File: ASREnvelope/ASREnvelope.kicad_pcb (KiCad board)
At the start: 2 copper layers, 40 parts, among them J1 GATE, J2 Power, J3 OUT, J4 INV OUT, U1 TL074, U2 TL072

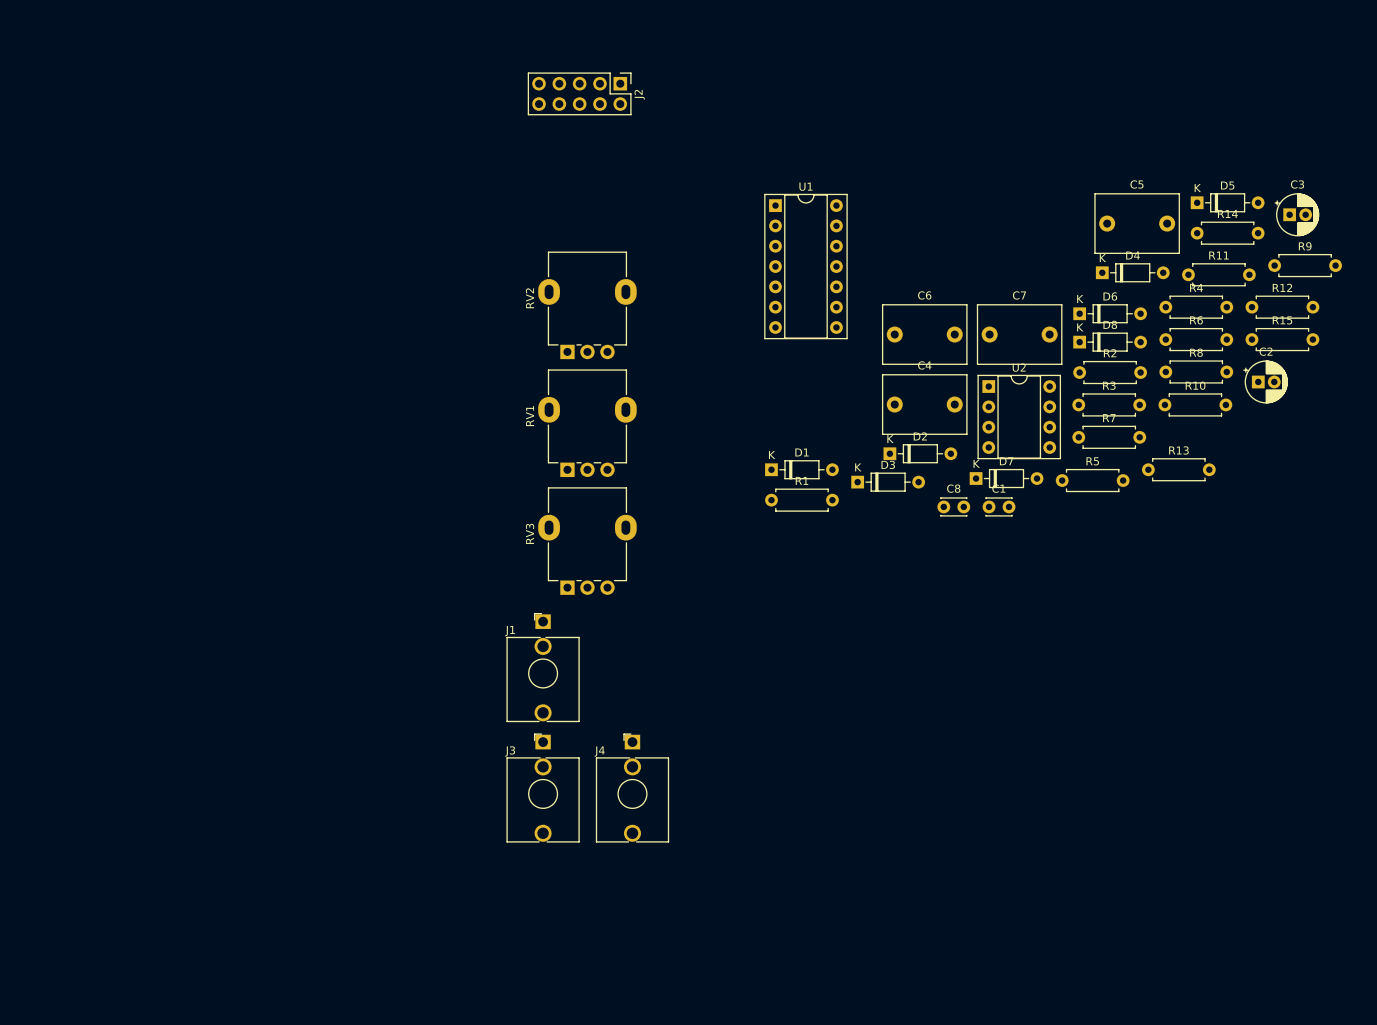
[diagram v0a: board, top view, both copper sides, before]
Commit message: move circuit to two boards
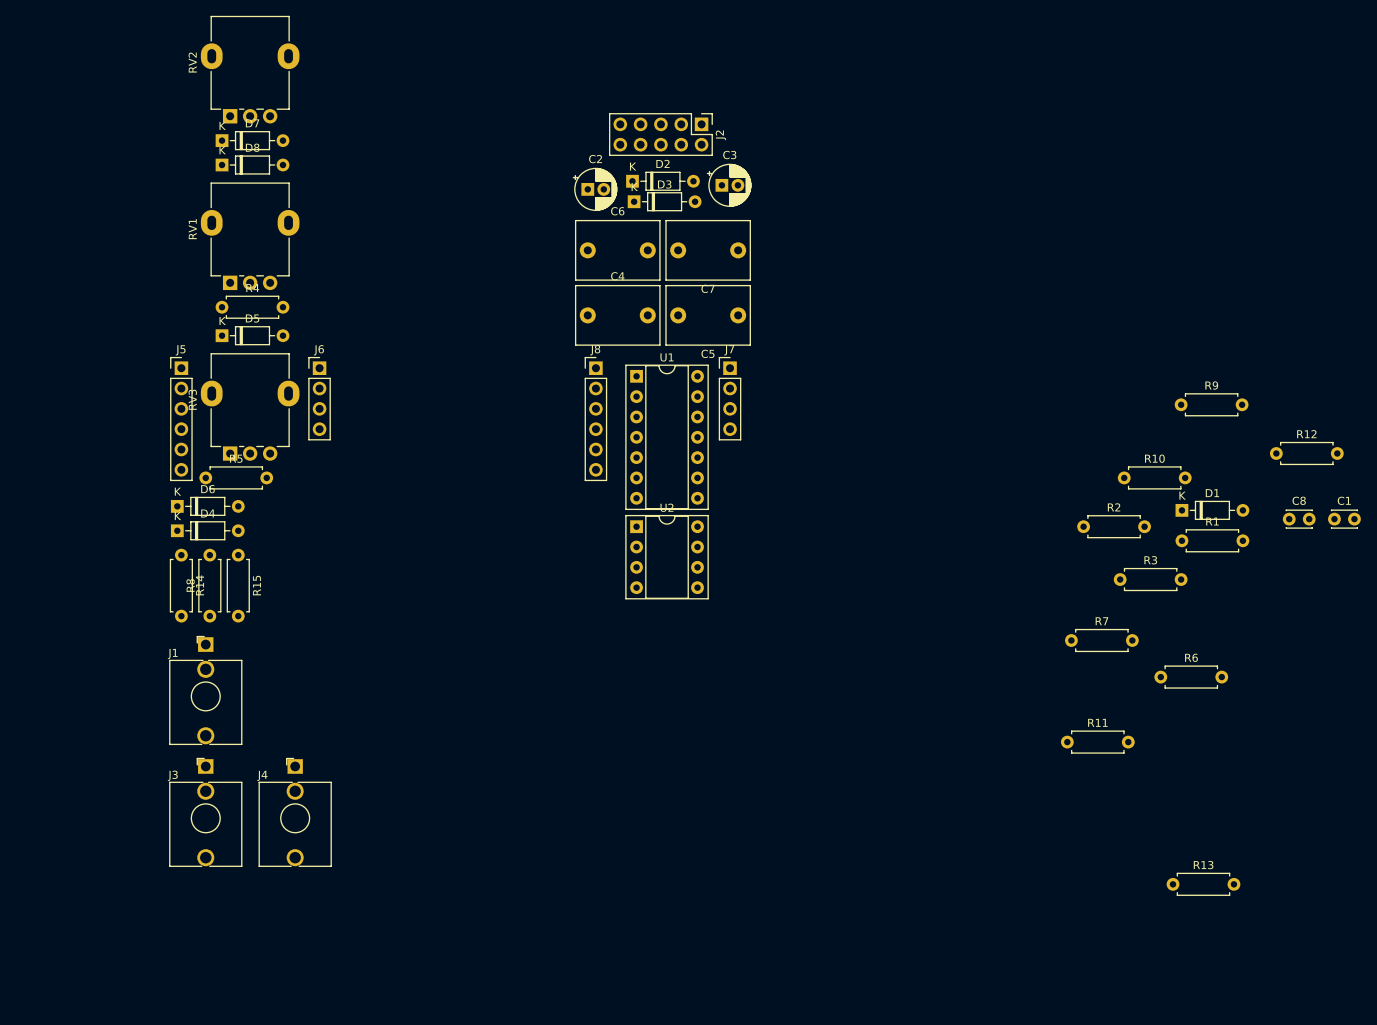
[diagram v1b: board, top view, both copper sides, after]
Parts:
- added J5: Conn_01x06_Male, Connector_PinHeader_2.54mm:PinHeader_1x06_P2.54mm_Vertical, F.Cu at (108.2, 79.2)
- added J6: Conn_01x04_Male, Connector_PinHeader_2.54mm:PinHeader_1x04_P2.54mm_Vertical, F.Cu at (125.5, 79.2)
- added J7: Conn_01x04_Female, Connector_PinHeader_2.54mm:PinHeader_1x04_P2.54mm_Vertical, F.Cu at (176.8, 79.2)
- added J8: Conn_01x06_Female, Connector_PinHeader_2.54mm:PinHeader_1x06_P2.54mm_Vertical, F.Cu at (160.0, 79.2)
- moved R14 133.2 mm to (108.2, 102.6), turned to 270 degrees
- moved R15 129.5 mm to (115.3, 102.6), turned to 270 degrees
- moved R8 123.3 mm to (111.8, 110.2), turned to 90 degrees
- moved D5 123.0 mm to (113.3, 75.2)
- moved D4 120.0 mm to (107.7, 99.6)
- moved R4 118.0 mm to (113.3, 71.6)
- moved D6 115.3 mm to (107.7, 96.5)
- moved D8 109.5 mm to (113.3, 53.8)
- moved R5 107.1 mm to (111.3, 93.0)
- moved D7 103.3 mm to (113.3, 50.8)
- moved C2 87.2 mm to (159.0, 56.9)
- moved C3 71.1 mm to (175.8, 56.4)
- moved R11 60.3 mm to (218.9, 126.0)
- moved R13 51.9 mm to (232.2, 143.8)
- moved D1 51.6 mm to (233.3, 97.0)
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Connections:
- net Earth renamed GroundA
- C1 pad 2: Net-(C1-Pad2) -> GateJackB
- C8 pad 1: Net-(C8-Pad1) -> Conn4B
- D4 pad 2: Net-(D4-Pad2) -> Switch3A
- D5 pad 2: Net-(D5-Pad2) -> Conn1A
- D6 pad 2: Net-(D6-Pad2) -> Switch1A
- J1 pad T: Net-(C1-Pad2) -> GateJackA
- R11 pad 1: Net-(R11-Pad1) -> OutJackB
- R13 pad 2: Net-(R13-Pad2) -> InvOutJackB'
- R14 pad 1: Net-(R11-Pad1) -> OutJackA
- R15 pad 1: Net-(R13-Pad2) -> InvOutJackA
- R4 pad 1: Net-(D4-Pad1) -> Switch3A
- R6 pad 2: Net-(D6-Pad2) -> Switch1B
- R8 pad 2: Net-(R8-Pad2) -> Conn3A
- RV2 pad 1: Net-(C8-Pad1) -> Conn4A
- RV2 pad 2: Net-(C8-Pad1) -> Conn4A
- RV3 pad 1: Net-(C8-Pad1) -> Conn4A
- RV3 pad 2: Net-(C8-Pad1) -> Conn4A
- U1 pad 1: Net-(D4-Pad2) -> Switch3B
- U1 pad 10: Net-(SW1-Pad2) -> Switch2B
- U1 pad 13: Net-(R11-Pad1) -> OutJackB
- U1 pad 14: Net-(D6-Pad2) -> Switch1B
- U1 pad 5: Net-(C1-Pad2) -> GateJackB
- U1 pad 7: Net-(D5-Pad2) -> Conn1B
- U1 pad 8: Net-(R8-Pad2) -> Conn3B
- U1 pad 9: Net-(R8-Pad2) -> Conn3B
- U2 pad 1: Net-(R11-Pad1) -> OutJackB
- U2 pad 2: Net-(R11-Pad1) -> OutJackB
- U2 pad 3: Net-(C8-Pad1) -> Conn4B
- U2 pad 7: Net-(R13-Pad2) -> InvOutJackB'

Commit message: add mult project
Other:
- net class Default removed

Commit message: rearrange a bunch of files
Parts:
- C1, C8: footprint Capacitor_THT:C_Disc_D3.0mm_W2.0mm_P2.50mm -> Capacitor_THT:C_Disc_D3.0mm_W1.6mm_P2.50mm
- C2, C3: footprint Capacitor_THT:CP_Radial_D5.0mm_P2.00mm -> Capacitor_THT:CP_Radial_D5.0mm_P2.50mm
- C4, C5, C6, C7: footprint Capacitor_THT:C_Rect_L10.3mm_W7.2mm_P7.50mm_MKS4 -> Capacitor_THT:C_Disc_D11.0mm_W5.0mm_P7.50mm
- D2, D3: footprint Diode_THT:D_DO-35_SOD27_P7.62mm_Horizontal -> Diode_THT:D_DO-41_SOD81_P7.62mm_Horizontal
- J1, J3, J4: footprint Connector_Audio:Jack_3.5mm_QingPu_WQP-PJ398SM_Vertical_CircularHoles -> pj398m:Jack_3.5mm_QingPu_WQP-PJ398SM_Vertical
- J2: footprint Connector_PinHeader_2.54mm:PinHeader_2x05_P2.54mm_Vertical -> pj398m:Jack_3.5mm_QingPu_WQP-PJ398SM_Vertical
- J7: footprint Connector_PinHeader_2.54mm:PinHeader_1x04_P2.54mm_Vertical -> Connector_PinSocket_2.54mm:PinSocket_1x04_P2.54mm_Vertical
- J8: footprint Connector_PinHeader_2.54mm:PinHeader_1x06_P2.54mm_Vertical -> Connector_PinSocket_2.54mm:PinSocket_1x06_P2.54mm_Vertical
- RV1, RV2, RV3: footprint Potentiometer_THT:Potentiometer_Alpha_RD901F-40-00D_Single_Vertical -> Potentiometer_THT:Potentiometer_Alpha_RD901F-40-00D_Single_Vertical_CircularHoles
- U1: footprint Package_DIP:DIP-14_W7.62mm_Socket -> Package_DIP:DIP-16_W7.62mm_Socket_LongPads
- U2: footprint Package_DIP:DIP-8_W7.62mm_Socket -> Package_DIP:DIP-8_W7.62mm_Socket_LongPads
- moved C8 120.8 mm to (125.9, 96.5)
- moved D1 89.8 mm to (145.2, 114.2)
- moved R5 87.3 mm to (195.0, 68.3)
- moved J3 75.9 mm to (163.6, 74.1)
- moved C7 75.6 mm to (122.2, 115.7), turned to 0 degrees
- moved D8 74.4 mm to (178.8, 89.0)
- moved D7 74.2 mm to (166.2, 102.7)
- moved R13 73.8 mm to (178.8, 92.8)
- moved D6 69.2 mm to (176.0, 85.4)
- moved R2 66.9 mm to (155.9, 114.6)
- moved R9 66.7 mm to (168.1, 98.3)
- moved R12 66.6 mm to (178.8, 96.8)
- moved D2 66.1 mm to (134.1, 114.6)
- moved R1 66.0 mm to (168.1, 90.7)
- moved J4 62.7 mm to (152.6, 74.1)
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
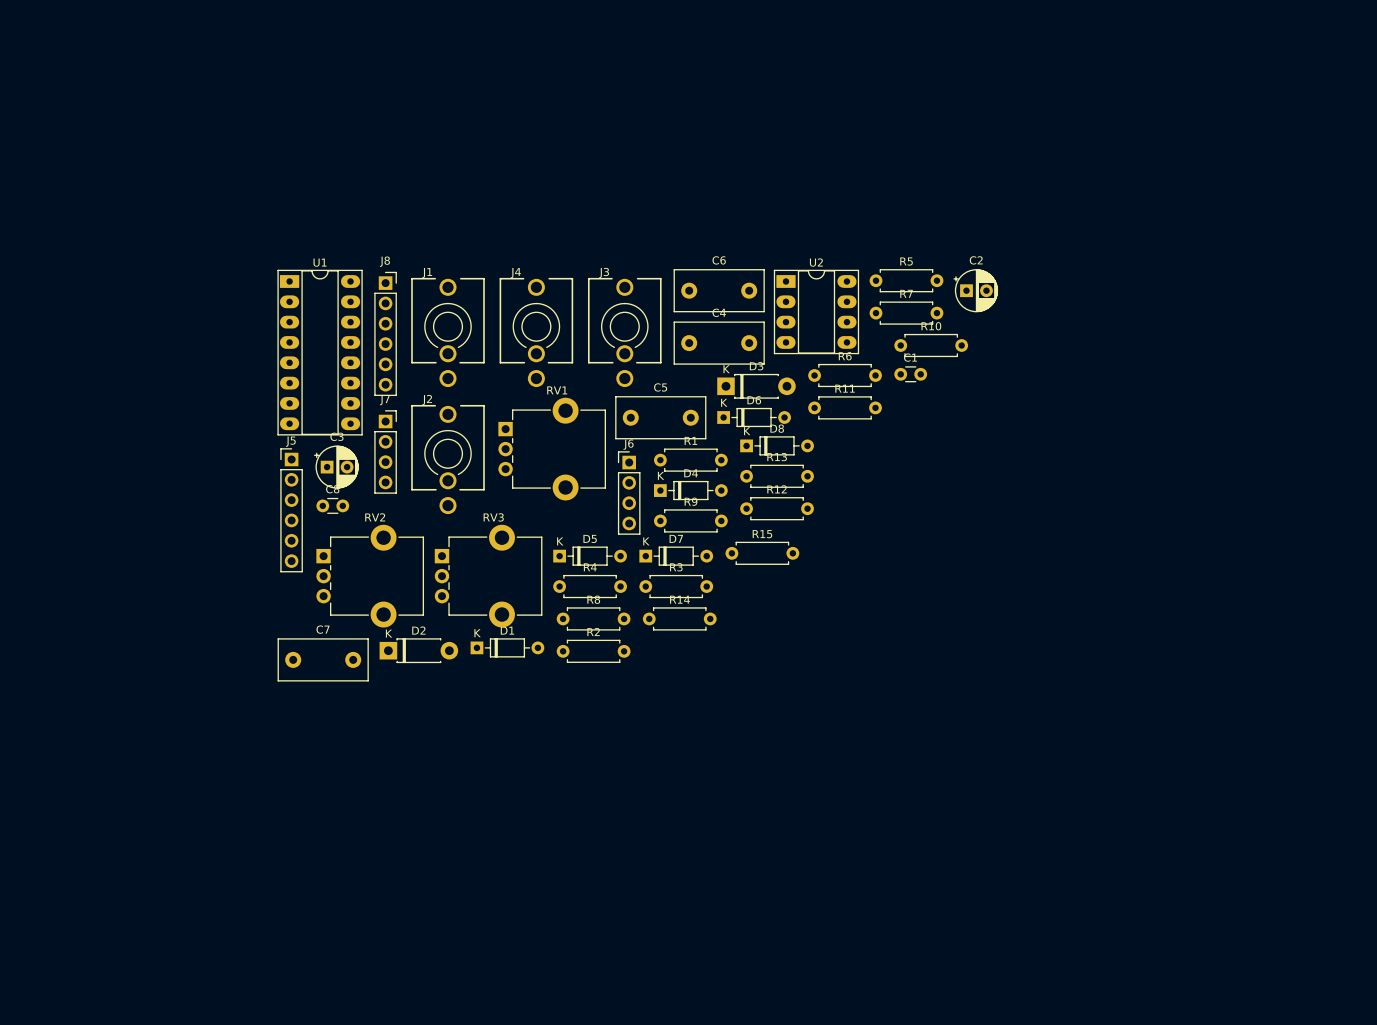
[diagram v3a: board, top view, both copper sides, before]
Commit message: add eurocad footprint library
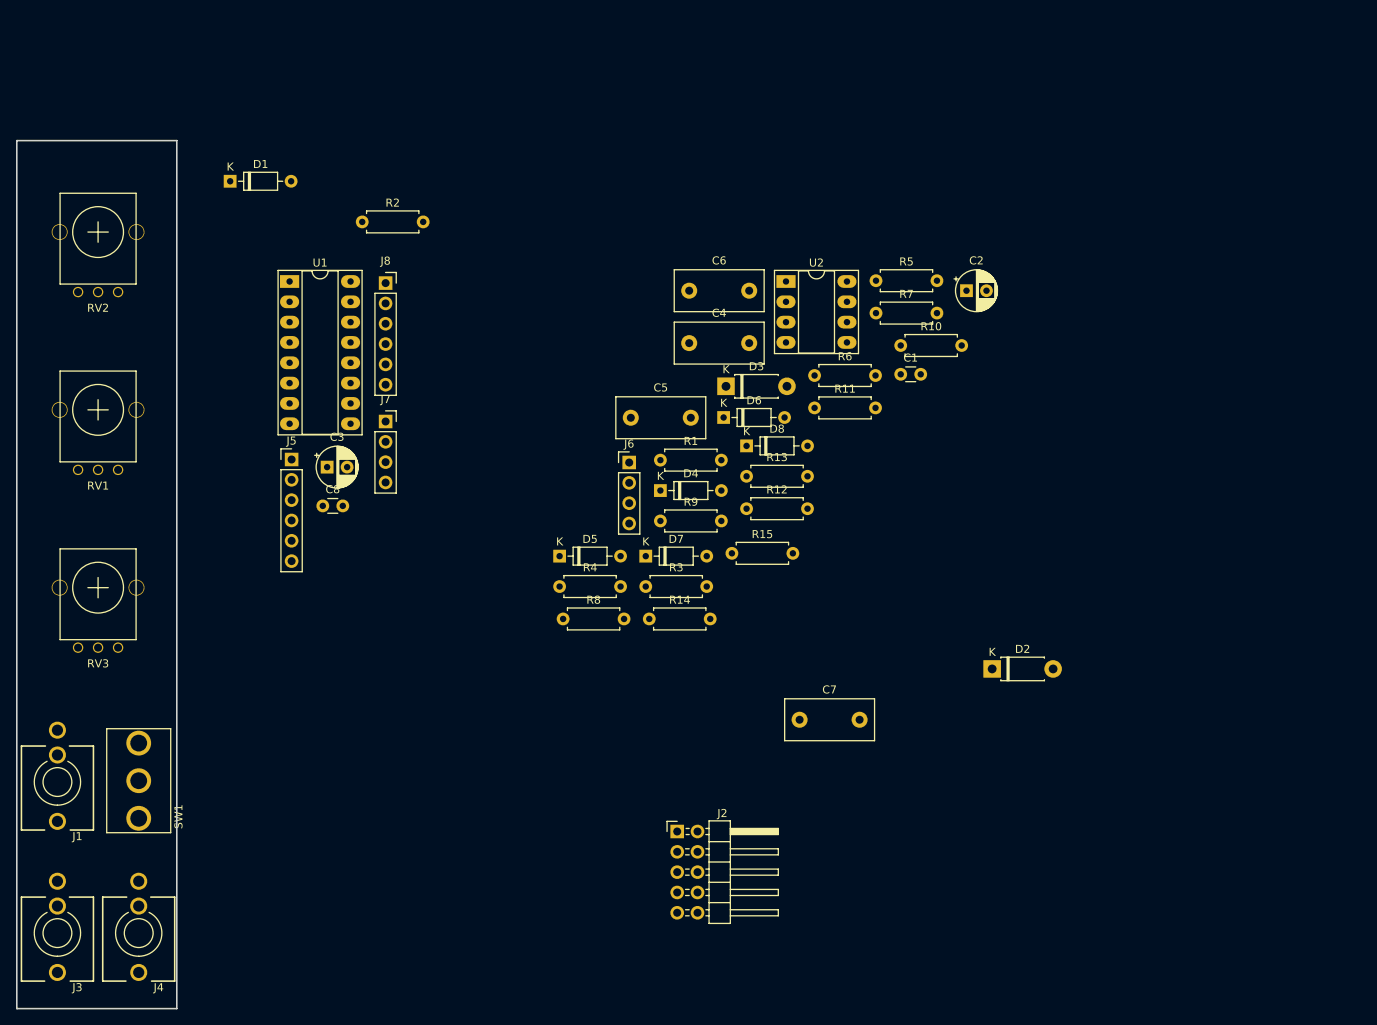
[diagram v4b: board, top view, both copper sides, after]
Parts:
- added SW1: SW_SPDT, Eurocad:SPDT toggle on-off-on, F.Cu at (102.9, 130.8)
- J2: footprint pj398m:Jack_3.5mm_QingPu_WQP-PJ398SM_Vertical -> Connector_PinHeader_2.54mm:PinHeader_2x05_P2.54mm_Horizontal
- RV1, RV2, RV3: footprint Potentiometer_THT:Potentiometer_Alpha_RD901F-40-00D_Single_Vertical_CircularHoles -> Eurocad:Alpha9mmPot
- moved J3 103.8 mm to (92.7, 149.9), turned to 180 degrees
- moved J4 90.6 mm to (102.9, 149.9), turned to 180 degrees
- moved D2 75.5 mm to (209.6, 116.8)
- moved J1 75.0 mm to (92.7, 131.0), turned to 180 degrees
- moved D1 66.0 mm to (114.3, 55.9)
- moved C7 63.7 mm to (185.5, 123.2)
- moved R2 59.3 mm to (130.8, 61.0)
- moved J2 55.2 mm to (170.2, 137.2)
- moved RV1 51.0 mm to (97.8, 84.5)
- moved RV2 49.4 mm to (97.8, 62.2)
- moved RV3 43.2 mm to (97.8, 106.7)
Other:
- board outline added: 20 x 108.5 mm
